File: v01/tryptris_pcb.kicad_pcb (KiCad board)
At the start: 2 copper layers, 298.8 x 122 mm, 141 parts, among them J1 USB_C_Receptacle_USB2.0, J2 I2C-L, J3 I2C-R, SW1 Reset, U1 ATmega32U4-AU, U2 MCP23017_SO, U4 HOLE, Y1 16Mhz

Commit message: More routing progress on RGB matrix
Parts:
- added C10: 0.47uF, Capacitor_SMD:C_0805_2012Metric, B.Cu at (264.1, 119.7)
- added C11: 0.47uF, Capacitor_SMD:C_0805_2012Metric, B.Cu at (105.7, 121.5)
- added C12: 0.47uF, Capacitor_SMD:C_0805_2012Metric, B.Cu at (101.7, 106.1)
- added C13: 0.47uF, Capacitor_SMD:C_0805_2012Metric, B.Cu at (108.4, 114.9)
- added C14: 0.1uF, Capacitor_SMD:C_0805_2012Metric, B.Cu at (249.4, 119.0)
- added C15: 0.1uF, Capacitor_SMD:C_0805_2012Metric, B.Cu at (268.1, 113.9)
- added C16: 0.1uF, Capacitor_SMD:C_0805_2012Metric, B.Cu at (260.6, 120.8)
- added C17: 0.1uF, Capacitor_SMD:C_0805_2012Metric, B.Cu at (102.2, 121.5)
- added C18: 0.1uF, Capacitor_SMD:C_0805_2012Metric, B.Cu at (104.2, 106.1)
- added C19: 0.1uF, Capacitor_SMD:C_0805_2012Metric, B.Cu at (108.4, 111.3)
- added C20: 0.47uF, Capacitor_SMD:C_0805_2012Metric, B.Cu at (249.4, 115.3)
- added C21: 0.47uF, Capacitor_SMD:C_0805_2012Metric, B.Cu at (97.9, 121.4)
- added C8: 0.47uF, Capacitor_SMD:C_0805_2012Metric, B.Cu at (253.8, 121.5)
- added C9: 0.47uF, Capacitor_SMD:C_0805_2012Metric, B.Cu at (268.1, 117.4)
- added D100: 6028 LED, Keebio-Parts:RGB_3528_Blue_Notch-MX, B.Cu at (277.8, 99.7)
- added D101: 6028 LED, Keebio-Parts:RGB_3528_Blue_Notch-MX, B.Cu at (296.8, 106.9)
- added D102: 6028 LED, Keebio-Parts:RGB_3528_Blue_Notch-MX, B.Cu at (315.8, 107.0)
- added D103: 6028 LED, Keebio-Parts:RGB_3528_Blue_Notch-MX, B.Cu at (118.4, 121.3)
- added D104: 6028 LED, Keebio-Parts:RGB_3528_Blue_Notch-MX, B.Cu at (139.7, 124.4)
- added D105: 6028 LED, Keebio-Parts:RGB_3528_Blue_Notch-MX, B.Cu at (159.1, 134.0)
- added D106: 6028 LED, Keebio-Parts:RGB_3528_Blue_Notch-MX, B.Cu at (193.1, 134.1)
- added D107: 6028 LED, Keebio-Parts:RGB_3528_Blue_Notch-MX, B.Cu at (212.3, 124.4)
- added D108: 6028 LED, Keebio-Parts:RGB_3528_Blue_Notch-MX, B.Cu at (233.7, 121.2)
- added D55: 6028 LED, Keebio-Parts:RGB_3528_Blue_Notch-MX, B.Cu at (36.2, 49.9)
- added D56: 6028 LED, Keebio-Parts:RGB_3528_Blue_Notch-MX, B.Cu at (55.3, 49.9)
- added D57: 6028 LED, Keebio-Parts:RGB_3528_Blue_Notch-MX, B.Cu at (74.3, 42.7)
- added D58: 6028 LED, Keebio-Parts:RGB_3528_Blue_Notch-MX, B.Cu at (93.2, 37.9)
- added D59: 6028 LED, Keebio-Parts:RGB_3528_Blue_Notch-MX, B.Cu at (112.3, 42.7)
- added D60: 6028 LED, Keebio-Parts:RGB_3528_Blue_Notch-MX, B.Cu at (131.2, 45.1)
- added D61: 6028 LED, Keebio-Parts:RGB_3528_Blue_Notch-MX, B.Cu at (220.7, 45.1)
- added D62: 6028 LED, Keebio-Parts:RGB_3528_Blue_Notch-MX, B.Cu at (239.9, 42.7)
- added D63: 6028 LED, Keebio-Parts:RGB_3528_Blue_Notch-MX, B.Cu at (258.9, 38.0)
- added D64: 6028 LED, Keebio-Parts:RGB_3528_Blue_Notch-MX, B.Cu at (277.7, 42.7)
- added D65: 6028 LED, Keebio-Parts:RGB_3528_Blue_Notch-MX, B.Cu at (296.8, 49.9)
- added D66: 6028 LED, Keebio-Parts:RGB_3528_Blue_Notch-MX, B.Cu at (315.7, 49.9)
- added D67: 6028 LED, Keebio-Parts:RGB_3528_Blue_Notch-MX, B.Cu at (36.2, 68.9)
- added D68: 6028 LED, Keebio-Parts:RGB_3528_Blue_Notch-MX, B.Cu at (55.2, 69.0)
- added D69: 6028 LED, Keebio-Parts:RGB_3528_Blue_Notch-MX, B.Cu at (74.3, 61.7)
- added D70: 6028 LED, Keebio-Parts:RGB_3528_Blue_Notch-MX, B.Cu at (93.2, 56.9)
- added D71: 6028 LED, Keebio-Parts:RGB_3528_Blue_Notch-MX, B.Cu at (112.3, 61.7)
- added D72: 6028 LED, Keebio-Parts:RGB_3528_Blue_Notch-MX, B.Cu at (131.2, 64.1)
- added D73: 6028 LED, Keebio-Parts:RGB_3528_Blue_Notch-MX, B.Cu at (220.6, 64.1)
- added D74: 6028 LED, Keebio-Parts:RGB_3528_Blue_Notch-MX, B.Cu at (239.8, 61.7)
- added D75: 6028 LED, Keebio-Parts:RGB_3528_Blue_Notch-MX, B.Cu at (258.8, 57.0)
- added D76: 6028 LED, Keebio-Parts:RGB_3528_Blue_Notch-MX, B.Cu at (277.8, 61.7)
- added D77: 6028 LED, Keebio-Parts:RGB_3528_Blue_Notch-MX, B.Cu at (296.9, 69.0)
- added D78: 6028 LED, Keebio-Parts:RGB_3528_Blue_Notch-MX, B.Cu at (315.8, 68.9)
- added D79: 6028 LED, Keebio-Parts:RGB_3528_Blue_Notch-MX, B.Cu at (36.2, 88.0)
- added D80: 6028 LED, Keebio-Parts:RGB_3528_Blue_Notch-MX, B.Cu at (55.3, 88.1)
- added D81: 6028 LED, Keebio-Parts:RGB_3528_Blue_Notch-MX, B.Cu at (74.3, 80.8)
- added D82: 6028 LED, Keebio-Parts:RGB_3528_Blue_Notch-MX, B.Cu at (112.3, 80.7)
- added D83: 6028 LED, Keebio-Parts:RGB_3528_Blue_Notch-MX, B.Cu at (131.2, 83.1)
- added D84: 6028 LED, Keebio-Parts:RGB_3528_Blue_Notch-MX, B.Cu at (93.2, 75.9)
- added D85: 6028 LED, Keebio-Parts:RGB_3528_Blue_Notch-MX, B.Cu at (220.7, 83.1)
- added D86: 6028 LED, Keebio-Parts:RGB_3528_Blue_Notch-MX, B.Cu at (239.8, 80.7)
- added D87: 6028 LED, Keebio-Parts:RGB_3528_Blue_Notch-MX, B.Cu at (258.8, 76.0)
- added D88: 6028 LED, Keebio-Parts:RGB_3528_Blue_Notch-MX, B.Cu at (296.8, 88.0)
- added D89: 6028 LED, Keebio-Parts:RGB_3528_Blue_Notch-MX, B.Cu at (315.8, 88.0)
- added D90: 6028 LED, Keebio-Parts:RGB_3528_Blue_Notch-MX, B.Cu at (277.8, 80.6)
- added D91: 6028 LED, Keebio-Parts:RGB_3528_Blue_Notch-MX, B.Cu at (36.2, 107.0)
- added D92: 6028 LED, Keebio-Parts:RGB_3528_Blue_Notch-MX, B.Cu at (55.3, 107.0)
- added D93: 6028 LED, Keebio-Parts:RGB_3528_Blue_Notch-MX, B.Cu at (74.3, 99.8)
- added D94: 6028 LED, Keebio-Parts:RGB_3528_Blue_Notch-MX, B.Cu at (93.3, 95.0)
- added D95: 6028 LED, Keebio-Parts:RGB_3528_Blue_Notch-MX, B.Cu at (112.3, 99.8)
- added D96: 6028 LED, Keebio-Parts:RGB_3528_Blue_Notch-MX, B.Cu at (131.2, 102.1)
- added D97: 6028 LED, Keebio-Parts:RGB_3528_Blue_Notch-MX, B.Cu at (220.7, 102.1)
- added D98: 6028 LED, Keebio-Parts:RGB_3528_Blue_Notch-MX, B.Cu at (239.8, 99.7)
- added D99: 6028 LED, Keebio-Parts:RGB_3528_Blue_Notch-MX, B.Cu at (258.8, 95.0)
- added R10: 100K, Resistor_SMD:R_0805_2012Metric, B.Cu at (249.3, 108.3)
- added R11: 100K, Resistor_SMD:R_0805_2012Metric, B.Cu at (91.9, 120.8)
- added R12: 100K, Resistor_SMD:R_0805_2012Metric, B.Cu at (88.4, 119.9)
- added R13: 20K, Resistor_SMD:R_0805_2012Metric, B.Cu at (257.2, 121.5)
- added R14: 20K, Resistor_SMD:R_0805_2012Metric, B.Cu at (108.4, 118.3)
- added R9: 100K, Resistor_SMD:R_0805_2012Metric, B.Cu at (249.3, 111.7)
- added U3: IS31FL3733-TQ, Package_QFP:TQFP-48-1EP_7x7mm_P0.5mm_EP5x5mm, B.Cu at (259.3, 113.2)
- added U4: IS31FL3733-TQ, Package_QFP:TQFP-48-1EP_7x7mm_P0.5mm_EP5x5mm, B.Cu at (96.1, 113.2)
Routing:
- net Left-SW1: track 0.00 -> 248.2 mm, vias 0 -> 2
- net Left-SW2: track 0.00 -> 225.4 mm, vias 0 -> 8
- net Left-SW3: track 0.00 -> 216.3 mm, vias 0 -> 11
- net Left-SW11: track 0.00 -> 192.8 mm, vias 0 -> 13
- net Left-SW8: track 0.00 -> 192.8 mm, vias 0 -> 14
- net Left-SW10: track 0.00 -> 187.9 mm, vias 0 -> 2
- net Left-SW12: track 0.00 -> 185.6 mm, vias 0 -> 8
- net Left-SW7: track 0.00 -> 178.5 mm, vias 0 -> 2
- net Left-SW9: track 0.00 -> 175.5 mm, vias 0 -> 4
- net Left-SW5: track 0.00 -> 170.7 mm, vias 0 -> 8
- net Left-SW4: track 0.00 -> 163.8 mm, vias 0 -> 2
- net Left-SW6: track 0.00 -> 160.9 mm, vias 0 -> 10
- net Left-CS1: track 0.00 -> 136.9 mm, vias 0 -> 5
- net SCL-L: track 46.9 -> 163.7 mm, vias 1 -> 4
- net Left-CS2: track 0.00 -> 114.1 mm, vias 0 -> 6
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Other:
- net class power: trace_width 0.375 -> 0.3

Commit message: Finished rough routing the left side.
Starting on the right.
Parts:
- turned C12 to 90 degrees
- turned C18 to 90 degrees
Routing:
- net Right-CS6: track 0.00 -> 133.4 mm, vias 0 -> 4
- net Right-SW2: track 0.00 -> 118.2 mm
- net Right-SW3: track 0.00 -> 114.6 mm, vias 0 -> 10
- net Right-SW1: track 0.00 -> 112.3 mm
- net Right-CS4: track 0.00 -> 74.3 mm, vias 0 -> 4
- net Right-CS1: track 0.00 -> 74.3 mm, vias 0 -> 4
- net Right-CS2: track 0.00 -> 74.1 mm, vias 0 -> 4
- net Right-CS5: track 0.00 -> 74.0 mm, vias 0 -> 4
- net +5V: track 192.5 -> 261.7 mm, vias 6 -> 10
- net Left-CS8: track 2.44 -> 69.6 mm, vias 1 -> 2
- net GND: track 245.2 -> 305.6 mm, vias 1 -> 4
- net Left-CS6: track 80.0 -> 123.5 mm, vias 5 -> 6
- net Right-SW5: track 0.00 -> 18.3 mm
- net Left-CS5: track 91.2 -> 104.3 mm, vias 7 -> 8
- net Col6: track 143.7 -> 151.4 mm
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
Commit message: Finish first draft of routing on both sides.
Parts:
- moved C8 8.24 mm to (245.6, 121.3)
- moved C15 5.49 mm to (271.5, 118.3), turned to 270 degrees
- moved R13 3.85 mm to (253.4, 122.0), turned to 180 degrees
- moved C14 2.35 mm to (249.1, 121.3), turned to 270 degrees
- moved C9 0.86 mm to (268.0, 118.3), turned to 270 degrees
- moved C20 0.18 mm to (249.4, 115.1)
- moved C16 0.10 mm to (260.5, 120.8)
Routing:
- net Right-SW11: track 0.00 -> 197.4 mm, vias 0 -> 2
- net Right-SW10: track 0.00 -> 196.5 mm, vias 0 -> 2
- net Right-SW12: track 0.00 -> 192.2 mm, vias 0 -> 11
- net Right-SW8: track 0.00 -> 165.9 mm, vias 0 -> 2
- net Right-SW7: track 0.00 -> 165.0 mm, vias 0 -> 2
- net Right-SW9: track 0.00 -> 160.4 mm, vias 0 -> 11
- net Right-SW4: track 0.00 -> 147.1 mm, vias 0 -> 2
- net Right-SW6: track 0.00 -> 145.3 mm, vias 0 -> 12
- net Right-SW5: track 18.3 -> 160.7 mm, vias 0 -> 2
- net VSS: track 70.8 -> 205.6 mm, vias 0 -> 4
- net VBUS: track 85.1 -> 217.4 mm, vias 4 -> 14
- net SCL-R: track 47.4 -> 163.2 mm, vias 1 -> 2
- net SDA-R: track 42.3 -> 154.0 mm, vias 1 -> 2
- net Right-SW1: track 112.3 -> 211.9 mm, vias 0 -> 2
- net Right-CS3: track 0.00 -> 97.1 mm, vias 0 -> 6
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
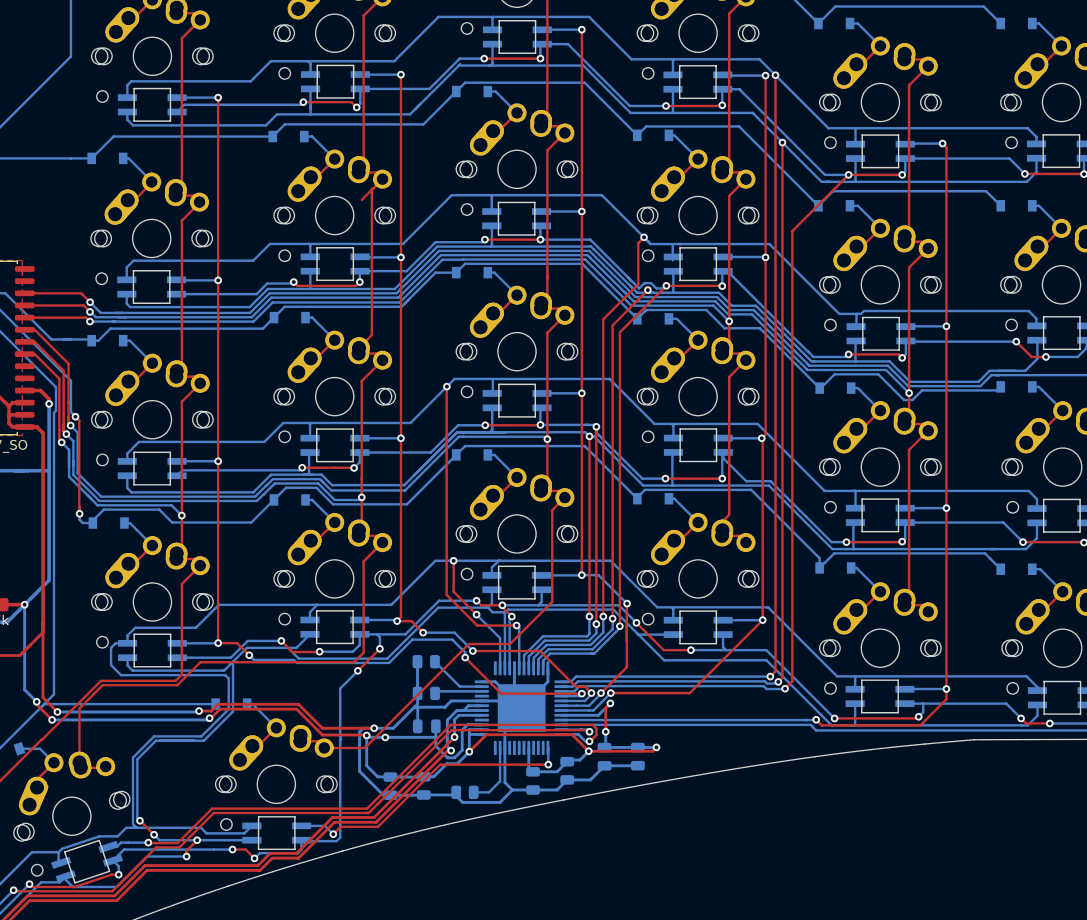
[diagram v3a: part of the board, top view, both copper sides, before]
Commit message: Tweak routing a bit.
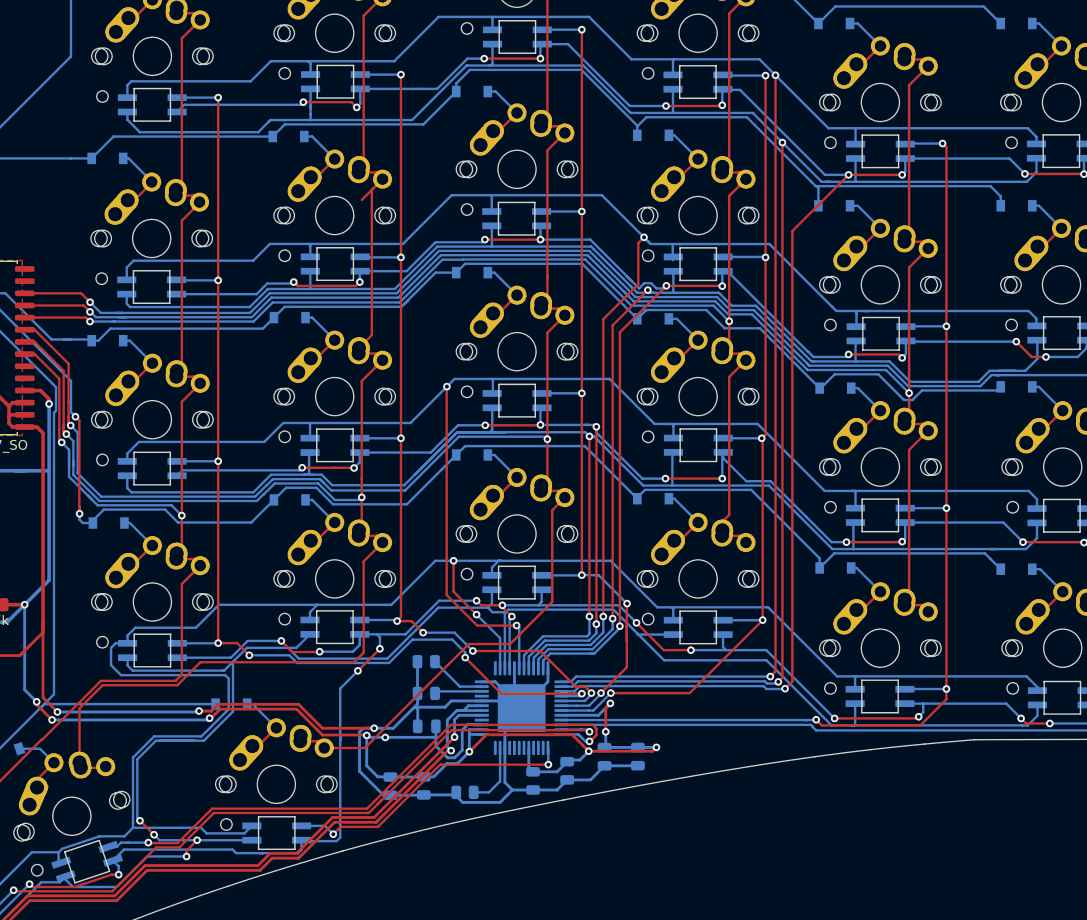
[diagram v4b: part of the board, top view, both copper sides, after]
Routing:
- net Row1-R: track 137.1 -> 141.1 mm
- net Right-SW7: track 165.0 -> 165.6 mm
- net Right-SW3: track 193.8 -> 193.6 mm, vias 17 -> 15
